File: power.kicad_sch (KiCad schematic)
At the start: 37 parts, among them J1 KYCON_KPJX-4S-S, J2 MicroFit_2x02, J3 24V/5A OUT, J3B1 DNI, Q1 BC847, Q2 IRF9540SPBF, Q3 BC857, SW1 DNI, U1 MC78M12BDTG, U2 MAX5035BUSA

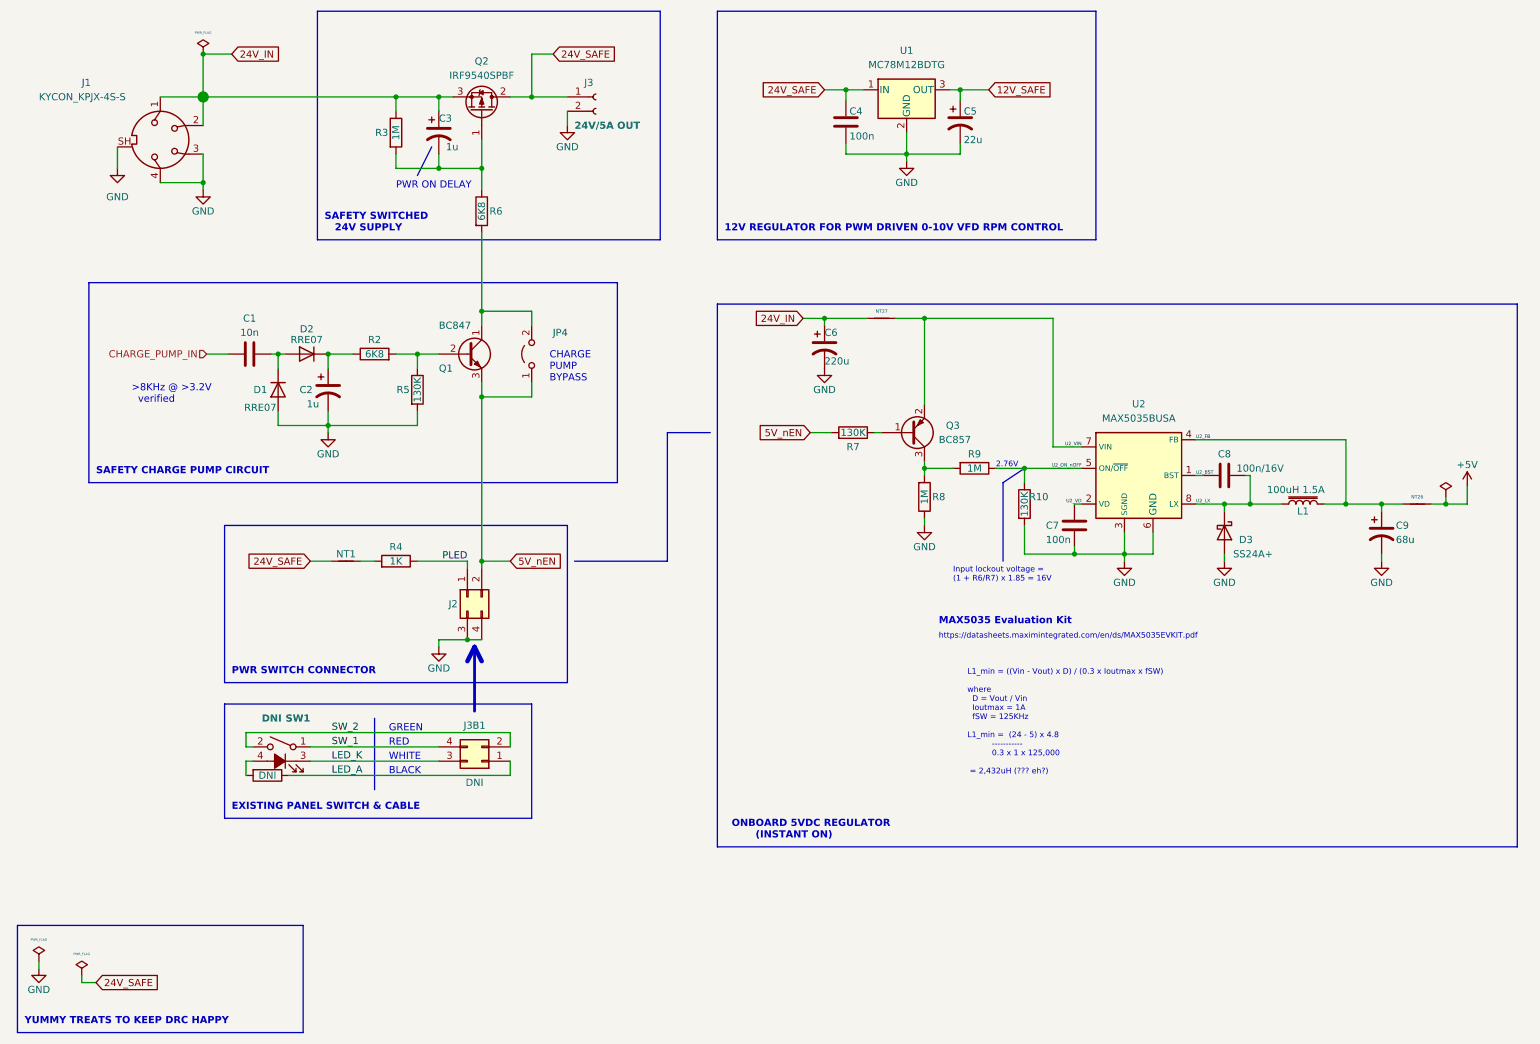
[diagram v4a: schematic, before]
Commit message: Routed power switching changes.
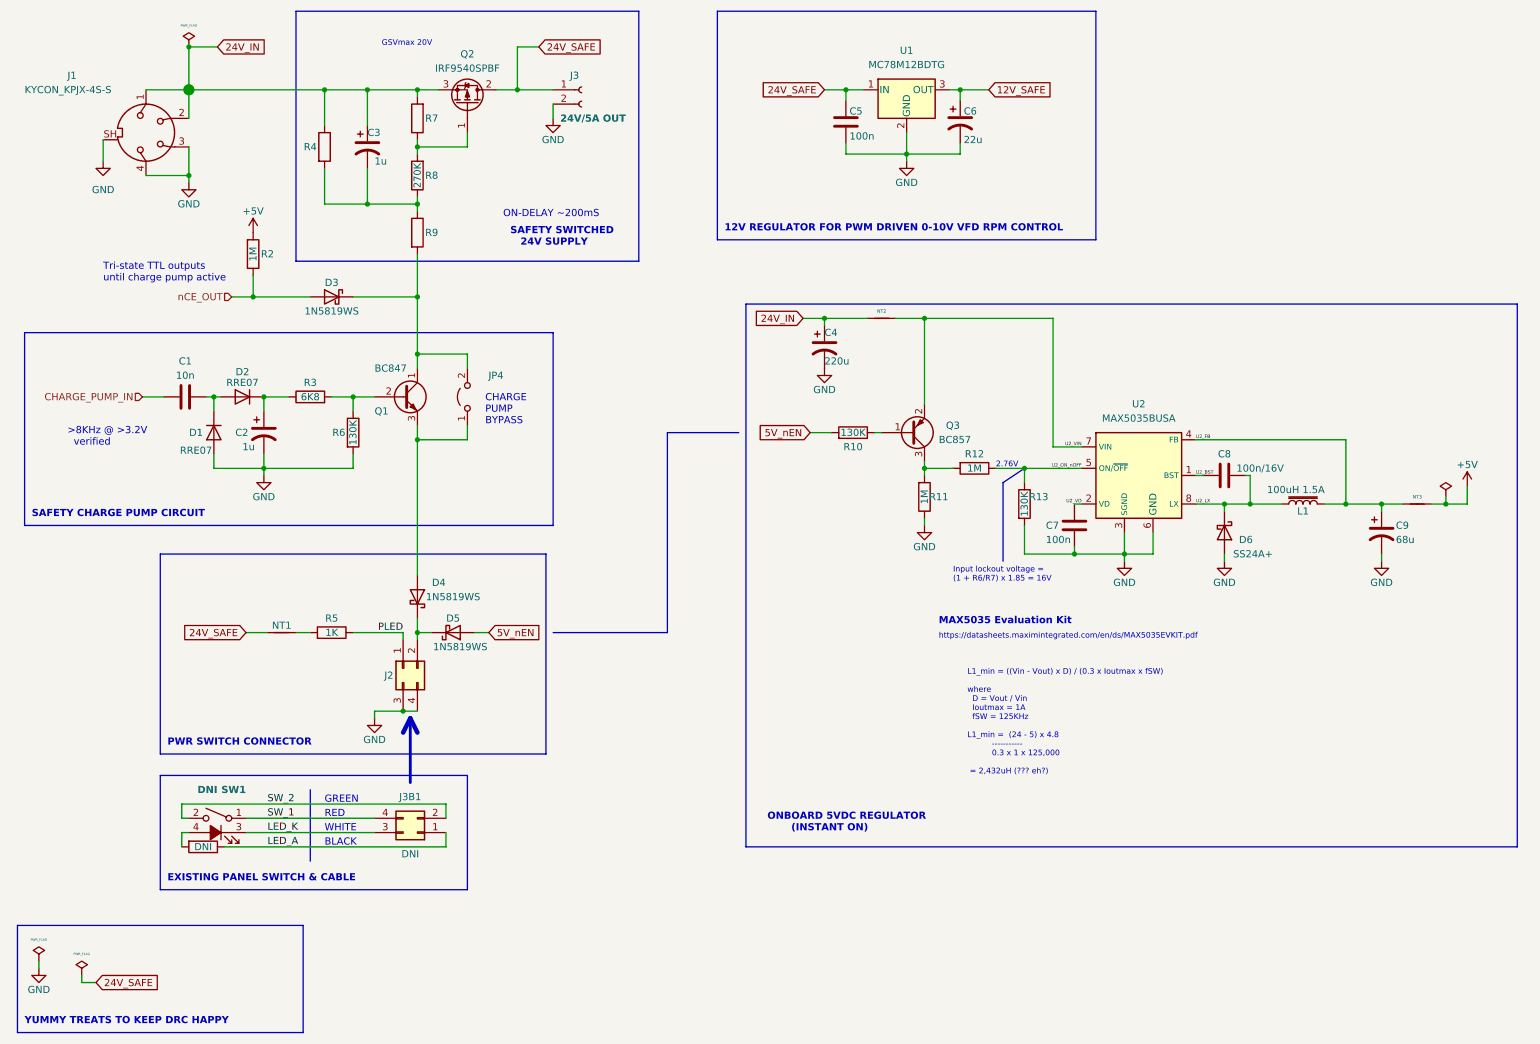
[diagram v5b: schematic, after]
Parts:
- added D3, D4, D5: 1N5819WS, Diode_SMD:D_SOD-323, symbol Device:D_Schottky
- added R2: 1M, Resistor_SMD:R_0603_1608Metric, symbol Device:R
- added R7: (no value), Resistor_SMD:R_0603_1608Metric, symbol Device:R
- added R8: 270K, Resistor_SMD:R_0603_1608Metric, symbol Device:R
- R4: renamed from R3; value 1M -> (none); footprint Resistor_SMD:R_0603_1608Metric -> (none)
- R9: renamed from R6; value 6K8 -> (none); footprint Resistor_SMD:R_0603_1608Metric -> (none)
- renumbered C6 to C4, C4 to C5, C5 to C6, D3 to D6, NT27 to NT2, NT26 to NT3, R7 to R10, R8 to R11, R9 to R12, R10 to R13, R2 to R3, R4 to R5, R5 to R6
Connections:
- net +5V: now also R2.2
- net 24V_IN: now also R7.2
- net 5V_nEN: now also D5.2 (A); no longer J2.2 (Pin_2), JP4.1 (A), Q1.3 (E)
- net at JP4.2 (B), Q1.1 (C), R9.2: now also D3.1 (K)
- net at C3.2, R4.2, R9.1: now also R8.1; no longer Q2.1 (G)
- new net: D4.2 (A), JP4.1 (A), Q1.3 (E)
- new net: Q2.1 (G), R7.1, R8.2
- new net: D4.1 (K), D5.1 (K), J2.2 (Pin_2)
- new net nCE_OUT: D3.2 (A), R2.1
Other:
- note added: "GSVmax 20V"
- note added: "ON-DELAY ~200mS"
- note added: "Tri-state TTL outputs until charge pump active"
- note removed: "PWR ON DELAY"
- moved on the sheet: C1, C2, C3, D1, D2, J1, J2, J3, J3B1, JP4, NT1, Q1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

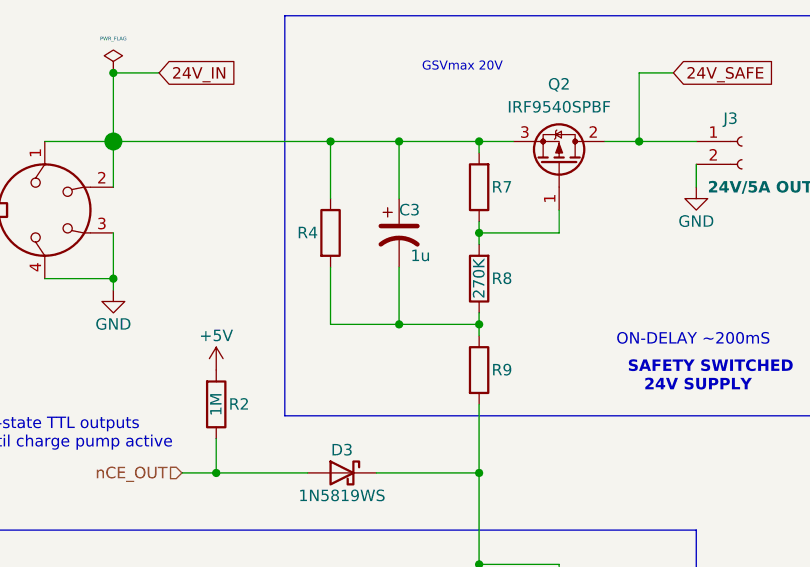
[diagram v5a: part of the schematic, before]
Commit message: More power supply and 5A ground return routing optimization.
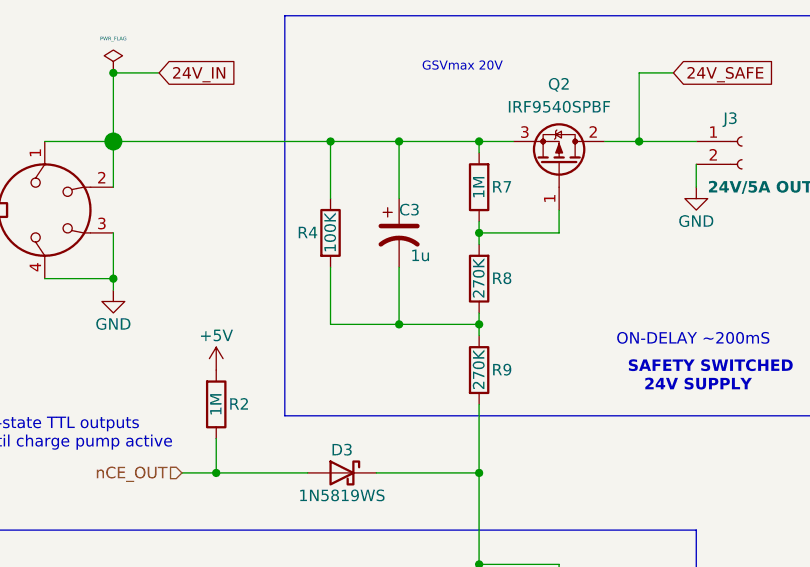
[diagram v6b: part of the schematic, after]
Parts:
- NT2: footprint -Project:NetTie-2_SMD_Pad0.5mm -> -Project:NetTie-2_SMD_Pad1.0mm
- R4: value (none) -> 100K; footprint (none) -> Resistor_SMD:R_0603_1608Metric
- R7: value (none) -> 1M
- R9: value (none) -> 270K; footprint (none) -> Resistor_SMD:R_0603_1608Metric
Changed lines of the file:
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@@
     (in_bom yes) (on_board yes)
     (property "Reference" "R4" (id 0) (at 66.04 38.1 0))
-    (property "Value" "" (id 1) (at 68.58 38.1 90))
-    (property "Footprint" "" (id 2) (at 66.802 38.1 90)
+    (property "Value" "100K" (id 1) (at 68.58 38.1 90))
+    (property "Footprint" "Resistor_SMD:R_0603_1608Metric" (id 2) (at 66.802 38.1 90)
       (effects (font (size 1.27 1.27)) hide)
     )
@@
     (in_bom yes) (on_board yes)
     (property "Reference" "R9" (id 0) (at 87.63 53.34 0))
-    (property "Value" "" (id 1) (at 85.09 53.34 90))
-    (property "Footprint" "" (id 2) (at 83.312 53.34 90)
+    (property "Value" "270K" (id 1) (at 85.09 53.34 90))
+    (property "Footprint" "Resistor_SMD:R_0603_1608Metric" (id 2) (at 83.312 53.34 90)
       (effects (font (size 1.27 1.27)) hide)
     )
@@
       (effects (font (size 1.27 1.27)) hide)
     )
-    (property "Footprint" "-Project:NetTie-2_SMD_Pad0.5mm" (id 2) (at 167.64 68.58 0)
+    (property "Footprint" "-Project:NetTie-2_SMD_Pad1.0mm" (id 2) (at 167.64 68.58 0)
       (effects (font (size 1.27 1.27)) hide)
     )
@@
     (in_bom yes) (on_board yes)
     (property "Reference" "R7" (id 0) (at 87.63 33.02 0))
-    (property "Value" "" (id 1) (at 85.09 33.02 90))
+    (property "Value" "1M" (id 1) (at 85.09 33.02 90))
     (property "Footprint" "Resistor_SMD:R_0603_1608Metric" (id 2) (at 86.868 33.02 90)
       (effects (font (size 1.27 1.27)) hide)

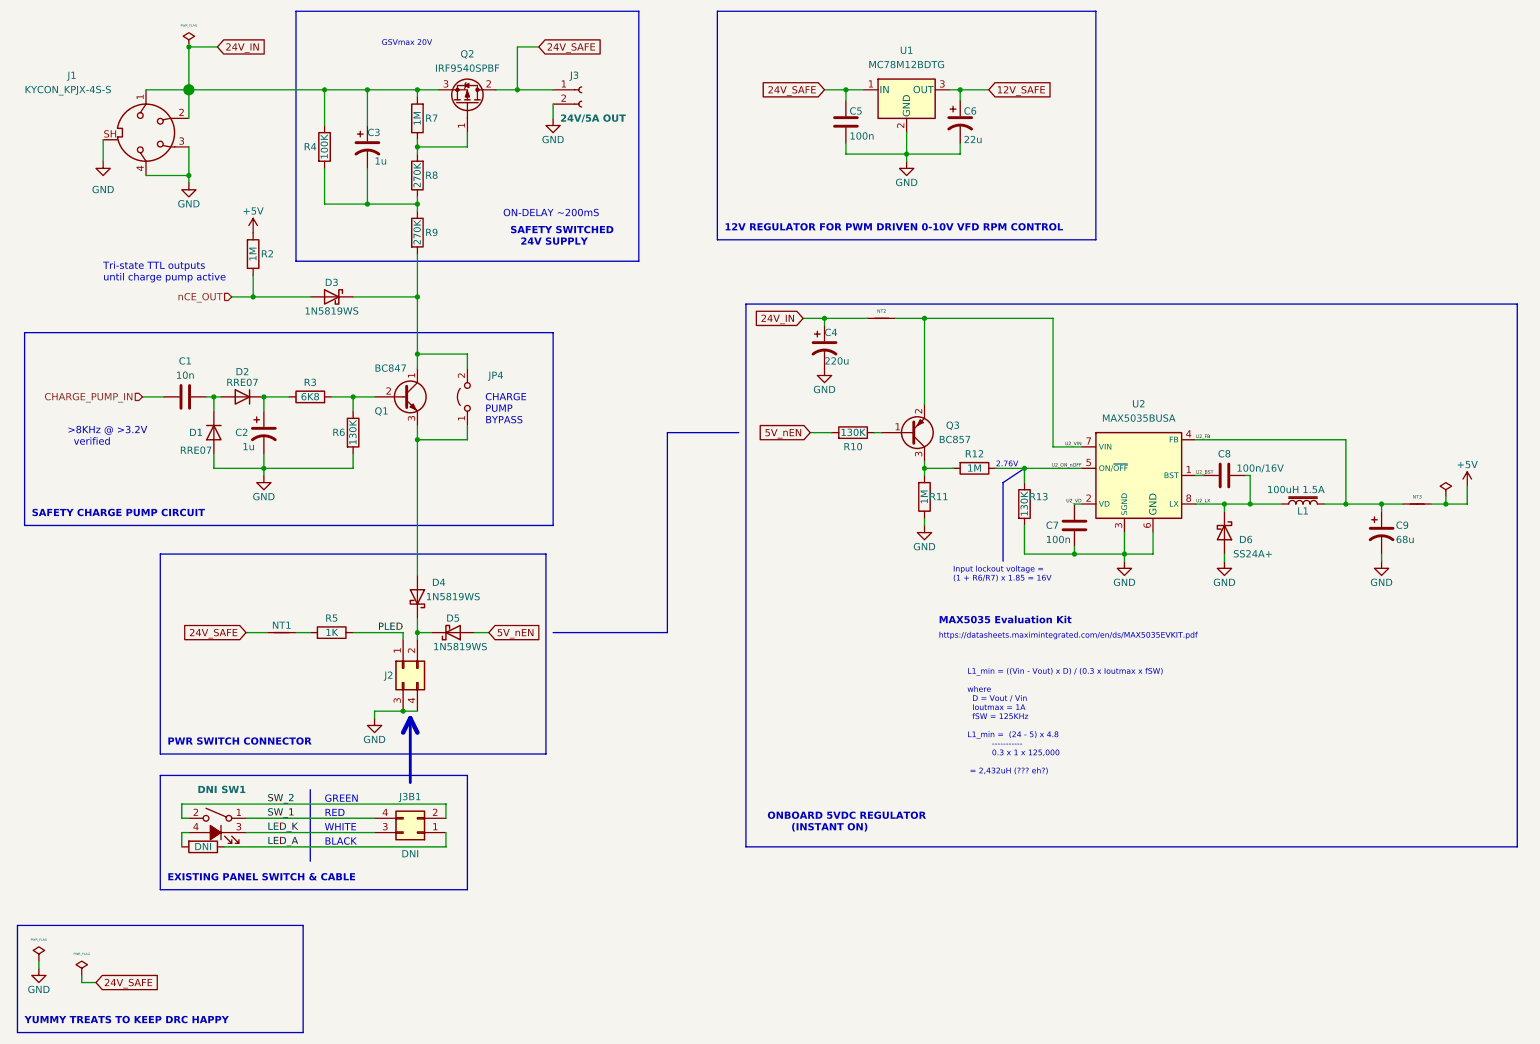
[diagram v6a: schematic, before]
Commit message: Tweaks and JLCPCB LCSC field name changes.
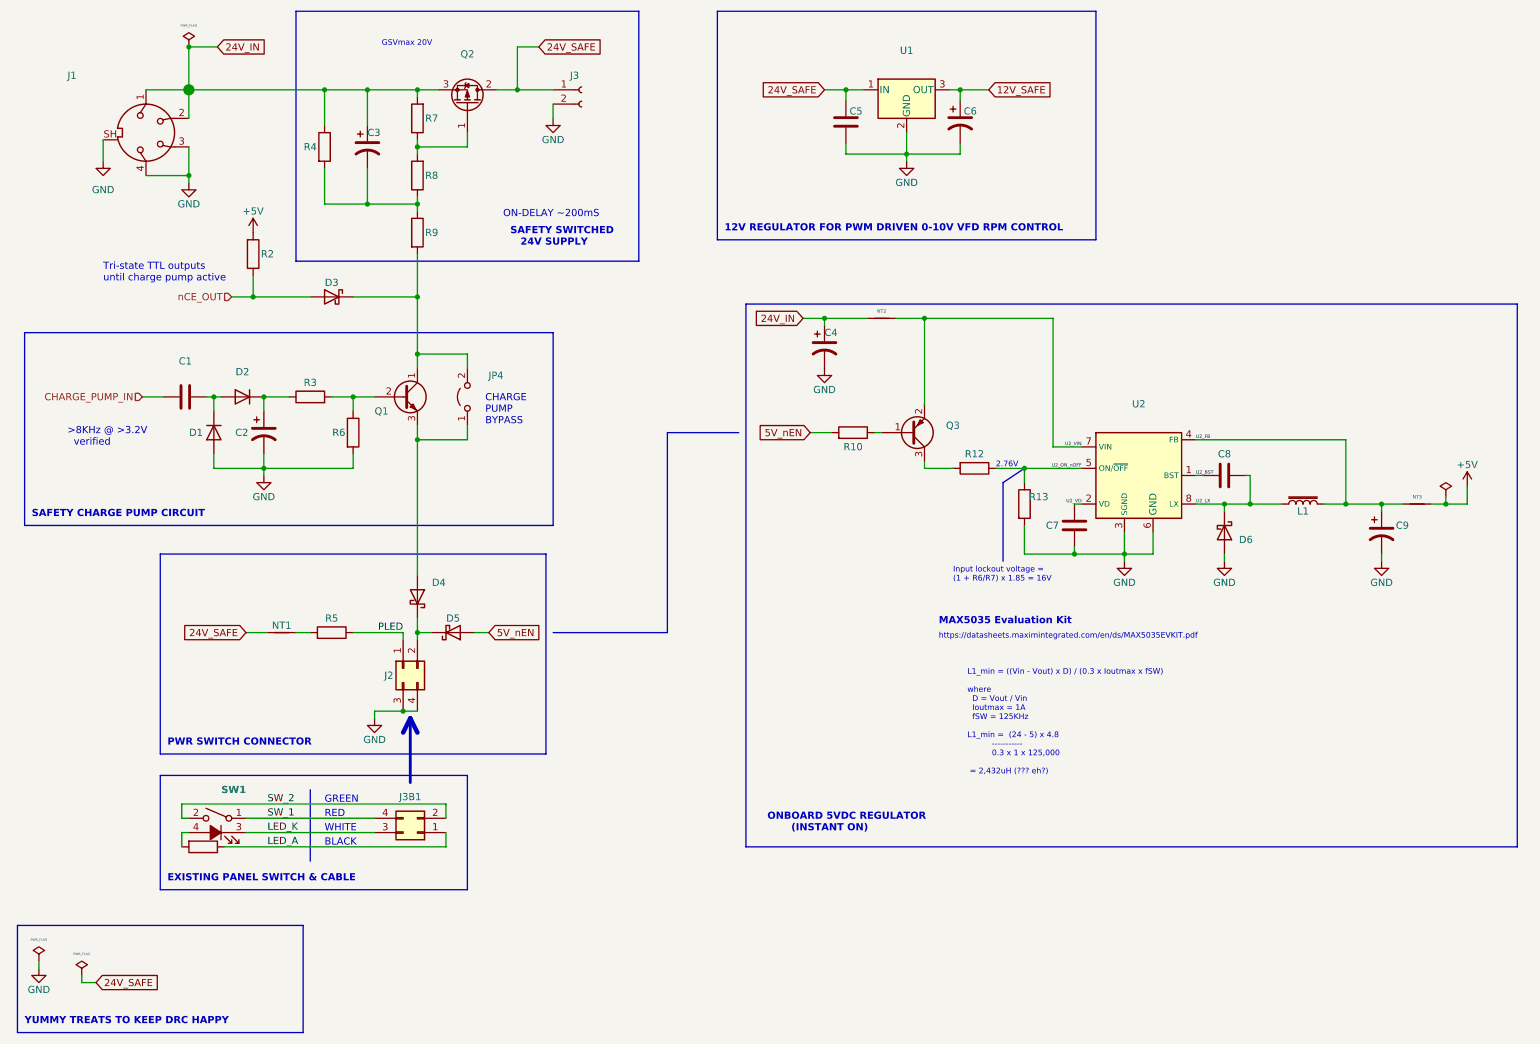
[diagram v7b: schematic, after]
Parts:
- removed R11: 1M, Resistor_SMD:R_0603_1608Metric, symbol Device:R
- C1: value 10n -> (none); footprint Capacitor_SMD:C_0603_1608Metric -> (none)
- C2, C3: value 1u -> (none); footprint Capacitor_SMD:C_0603_1608Metric -> (none)
- C4: value 220u -> (none); footprint Capacitor_SMD:CP_Elec_8x10.5 -> (none)
- C5, C7: value 100n -> (none); footprint Capacitor_SMD:C_0603_1608Metric -> (none)
- C6: value 22u -> (none); footprint Capacitor_SMD:C_0603_1608Metric -> (none)
- C8: value 100n/16V -> (none); footprint Capacitor_SMD:C_0603_1608Metric -> (none)
- C9: value 68u -> (none); footprint Capacitor_SMD:CP_Elec_6.3x7.7 -> (none)
- D1, D2: value RRE07 -> (none); footprint Diode_SMD:D_SOD-323_HandSoldering -> (none)
- D3, D4, D5: value 1N5819WS -> (none); footprint Diode_SMD:D_SOD-323 -> (none); JLCPART C191023 -> (none); LCSC (none) -> C191023
- D6: value SS24A+ -> (none); footprint Diode_SMD:D_SMA -> (none)
- J1: value KYCON_KPJX-4S-S -> (none); footprint -Project:KYCON_KPJX-4S-S -> (none)
- J2: value MicroFit_2x02 -> (none); footprint Connector_Molex:Molex_Micro-Fit_3.0_43045-0412_2x02_P3.00mm_Vertical -> (none)
- J3: value 24V/5A OUT -> (none); footprint TerminalBlock_RND:TerminalBlock_RND_205-00232_1x02_P5.08mm_Horizontal -> (none)
- J3B1, R1, SW1: value DNI -> (none)
- JP4: value Jumper_2_Bridged -> (none); footprint Connector_PinHeader_2.54mm:PinHeader_2x01_P2.54mm_Vertical -> (none)
- L1: value 100uH 1.5A -> (none); footprint Inductor_SMD:L_12x12mm_H6mm -> (none)
- NT1: value DNI -> (none); footprint -Project:NetTie-2_SMD_Pad0.3mm -> (none)
- NT2, NT3: value NetTie_2 -> (none); footprint -Project:NetTie-2_SMD_Pad1.0mm -> (none)
- Q1: value BC847 -> (none); footprint Package_TO_SOT_SMD:SOT-23 -> (none)
- Q2: value IRF9540SPBF -> (none); footprint Package_TO_SOT_SMD:TO-263-2 -> (none)
- Q3: value BC857 -> (none); footprint Package_TO_SOT_SMD:SOT-23 -> (none)
- R10, R13, R6: value 130K -> (none); footprint Resistor_SMD:R_0603_1608Metric -> (none)
- R12, R2, R7: value 1M -> (none); footprint Resistor_SMD:R_0603_1608Metric -> (none)
- R3: value 6K8 -> (none); footprint Resistor_SMD:R_0603_1608Metric -> (none)
- R4: value 100K -> (none); footprint Resistor_SMD:R_0603_1608Metric -> (none)
- R5: value 1K -> (none); footprint Resistor_SMD:R_0603_1608Metric -> (none)
- R8, R9: value 270K -> (none); footprint Resistor_SMD:R_0603_1608Metric -> (none)
- U1: value MC78M12BDTG -> (none); footprint Package_TO_SOT_SMD:TO-252-2 -> (none)
- U2: value MAX5035BUSA -> (none); footprint Package_SO:SOIC-8_3.9x4.9mm_P1.27mm -> (none)
